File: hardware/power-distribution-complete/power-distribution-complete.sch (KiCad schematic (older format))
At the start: 2 parts, among them J1 12V, J2 GND

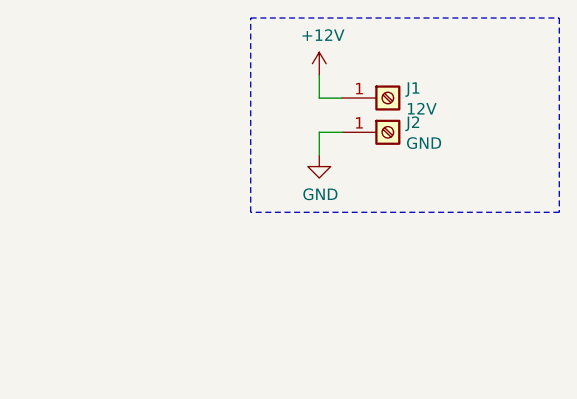
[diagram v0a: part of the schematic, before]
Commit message: Updated the power distribution schematic and pcb
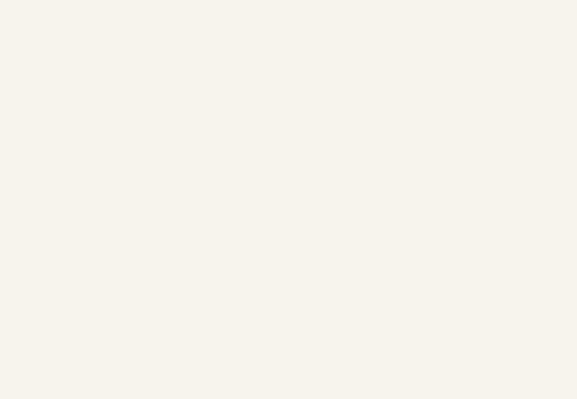
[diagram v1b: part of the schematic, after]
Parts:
- removed J1: 12V, Private:M5_7461383, symbol Connector:Screw_Terminal_01x01
- removed J2: GND, Private:M5_7461383, symbol Connector:Screw_Terminal_01x01
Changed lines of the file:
@@
 Comment4 ""
 $EndDescr
-Wire Notes Line
-	16950 750  18300 750
-Wire Notes Line
-	18300 1600 16950 1600
-Wire Notes Line
-	16950 1600 16950 750
-Wire Notes Line
-	18300 750  18300 1600
-$Comp
-L Connector:Screw_Terminal_01x01 J1
-U 1 1 5F050E2F
-P 17550 1100
-F 0 "J1" H 17630 1142 50  0000 L CNN
-F 1 "12V" H 17630 1051 50  0000 L CNN
-F 2 "Private:M5_7461383" H 17550 1100 50  0001 C CNN
-F 3 "~" H 17550 1100 50  0001 C CNN
-	1    17550 1100
-	1    0    0    -1
-$EndComp
-$Comp
-L Connector:Screw_Terminal_01x01 J2
-U 1 1 5F051827
-P 17550 1250
-F 0 "J2" H 17630 1292 50  0000 L CNN
-F 1 "GND" H 17630 1201 50  0000 L CNN
-F 2 "Private:M5_7461383" H 17550 1250 50  0001 C CNN
-F 3 "~" H 17550 1250 50  0001 C CNN
-	1    17550 1250
-	1    0    0    -1
-$EndComp
-$Comp
-L power:+12V #PWR01
-U 1 1 5F0520D2
-P 17250 1000
-F 0 "#PWR01" H 17250 850 50  0001 C CNN
-F 1 "+12V" H 17265 1173 50  0000 C CNN
-F 2 "" H 17250 1000 50  0001 C CNN
-F 3 "" H 17250 1000 50  0001 C CNN
-	1    17250 1000
-	1    0    0    -1
-$EndComp
-Wire Wire Line
-	17250 1000 17250 1100
-Wire Wire Line
-	17250 1100 17350 1100
-$Comp
-L power:GND #PWR02
-U 1 1 5F0538AE
-P 17250 1350
-F 0 "#PWR02" H 17250 1100 50  0001 C CNN
-F 1 "GND" H 17255 1177 50  0000 C CNN
-F 2 "" H 17250 1350 50  0001 C CNN
-F 3 "" H 17250 1350 50  0001 C CNN
-	1    17250 1350
-	1    0    0    -1
-$EndComp
-Wire Wire Line
-	17350 1250 17250 1250
-Wire Wire Line
-	17250 1250 17250 1350
 $Sheet
 S 5000 3500 1500 1000
